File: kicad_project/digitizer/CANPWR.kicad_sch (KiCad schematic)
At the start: 12 parts, among them IC201 MAX3059ASA+T UPSTREAM, IC202 MAX3059ASA+T DOWNSTREAM, IC203 MAX6035AAUR50+T, IC204 MAX6043BAUT33+T, J201 UP_CONN DT15-4P, J202 DOWN_CONN DT06-4S

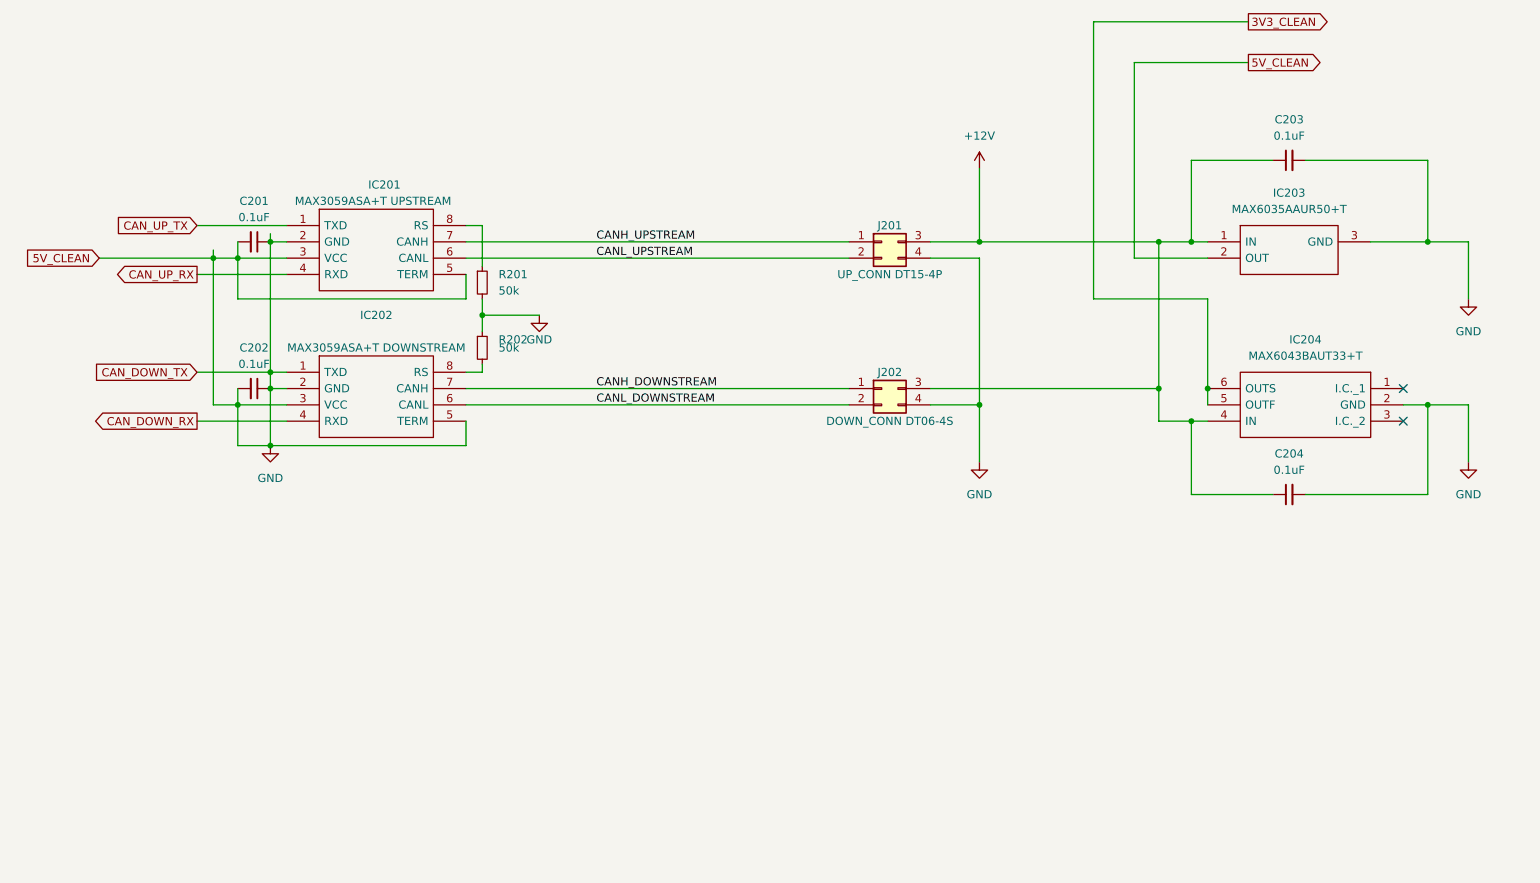
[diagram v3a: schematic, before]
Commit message: added GPIO lines, LED, other small changes
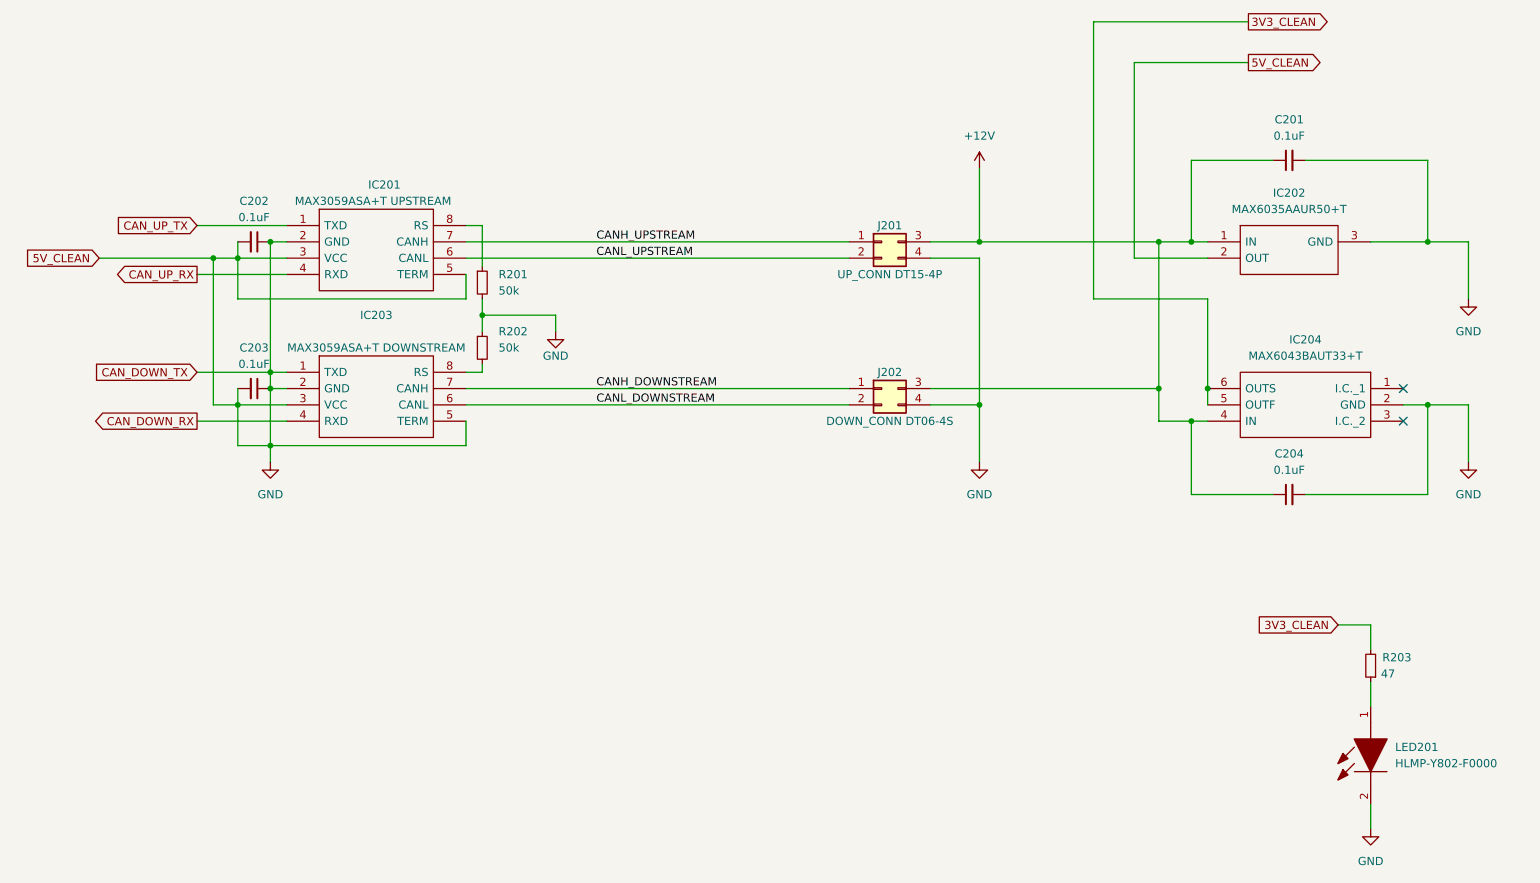
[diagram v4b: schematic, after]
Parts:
- added LED201: HLMP-Y802-F0000, HLMPY802F0000, symbol SamacSys_Parts:HLMP-Y802-F0000
- added R203: 47, Resistor_SMD:R_2512_6332Metric_Pad1.40x3.35mm_HandSolder, symbol Device:R_Small
- renumbered C203 to C201, C201 to C202, C202 to C203, IC203 to IC202, IC202 to IC203
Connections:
- net 3V3_CLEAN: now also R203.2
- net GND: now also LED201.2
- new net: LED201.1, R203.1

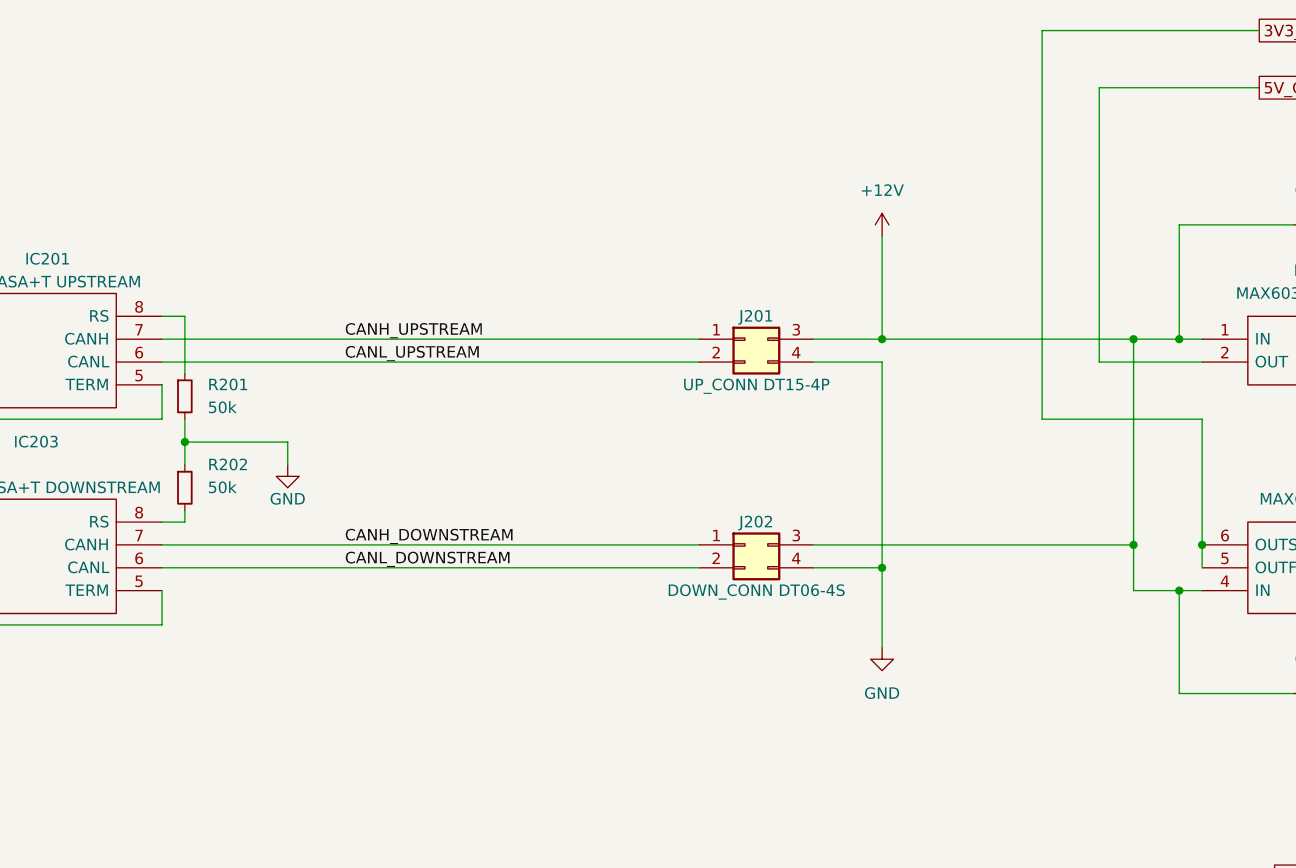
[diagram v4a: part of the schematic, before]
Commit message: added proper connector symbols and footprints for M12 and DT15 (digital upstream) connectors
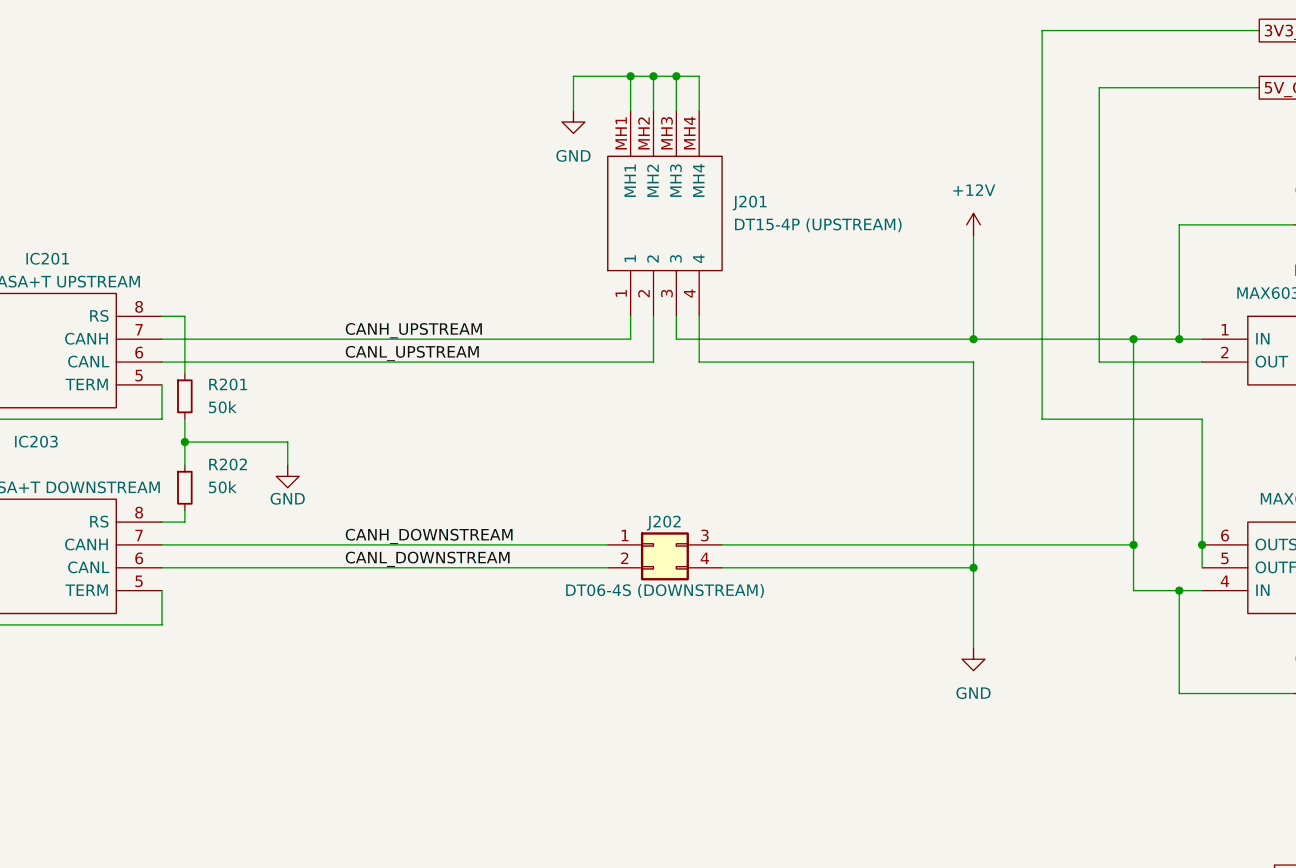
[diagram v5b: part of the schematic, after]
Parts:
- removed J201: UP_CONN DT15-4P, symbol Connector_Generic:Conn_02x02_Top_Bottom
- added J201: DT15-4P (UPSTREAM), DT154P, symbol SamacSys_Parts:DT15-4P
- J202: value DOWN_CONN DT06-4S -> DT06-4S (DOWNSTREAM)
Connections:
- net +12V: now also J201.3
- net CANH_UPSTREAM: now also J201.1
- net CANL_UPSTREAM: now also J201.2
- net GND: now also J201.4, J201.MH1, J201.MH2, J201.MH3, J201.MH4
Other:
- moved on the sheet: J202

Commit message: updated schematic to include terminal blocks for the analog M12 connectors and the downstream CANPWR connector
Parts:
- J202: footprint (none) -> SamacSys_Parts:1935187
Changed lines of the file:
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@@
     (property "Reference" "J202" (id 0) (at 151.13 81.28 0))
     (property "Value" "DT06-4S (DOWNSTREAM)" (id 1) (at 151.13 88.9 0))
-    (property "Footprint" "" (id 2) (at 149.86 83.82 0)
+    (property "Footprint" "SamacSys_Parts:1935187" (id 2) (at 149.86 83.82 0)
       (effects (font (size 1.27 1.27)) hide)
     )

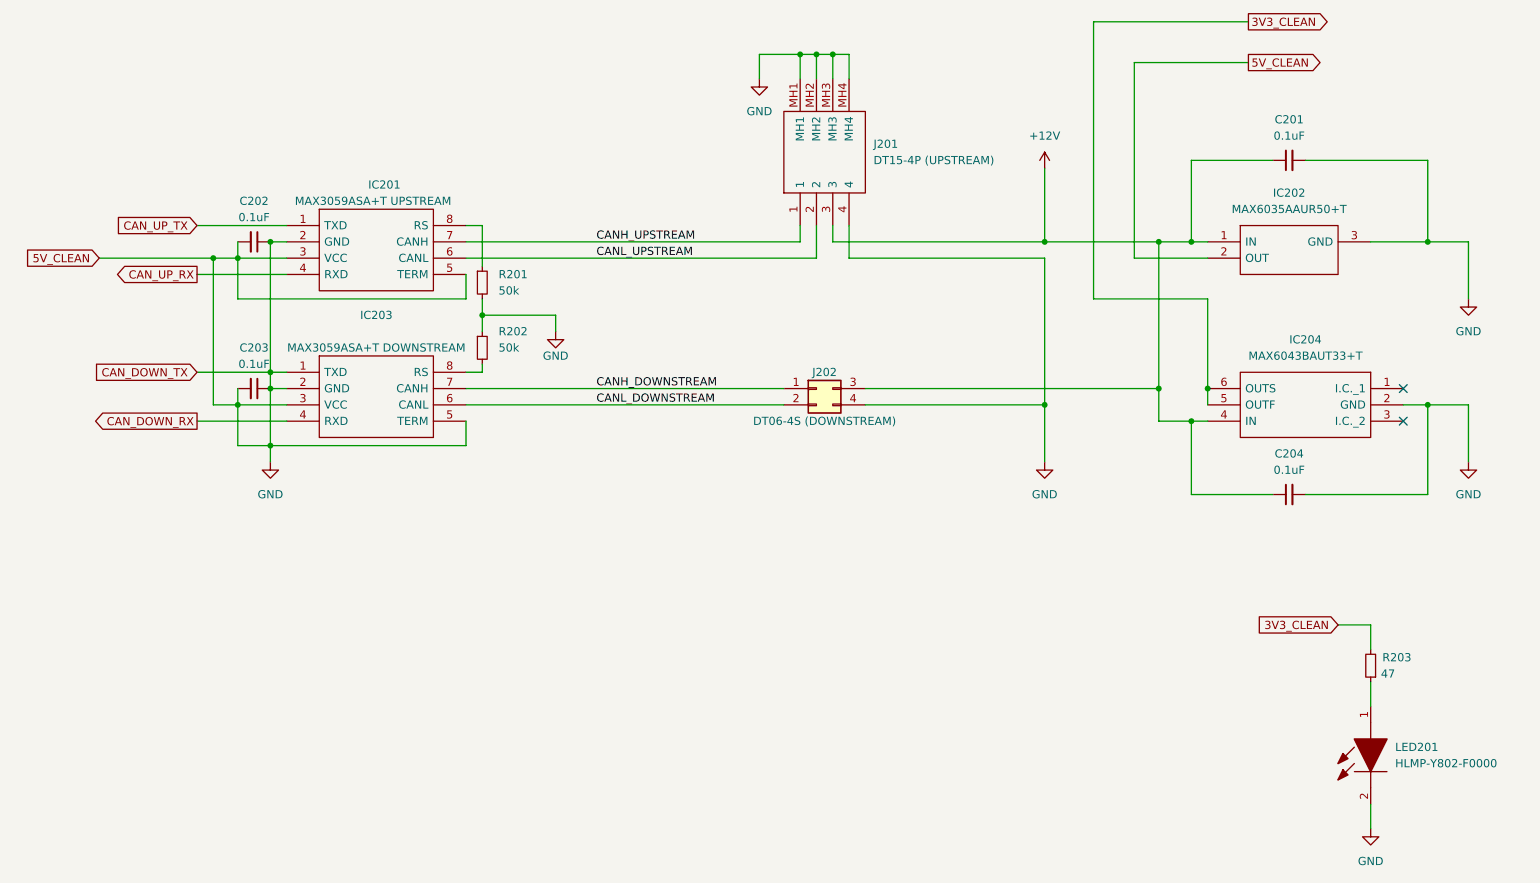
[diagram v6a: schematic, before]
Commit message: cleared ALL errors from electrical rules check; had to explicitly define a bunch of pins, and remove a few bugs (shorted lines, etc.)
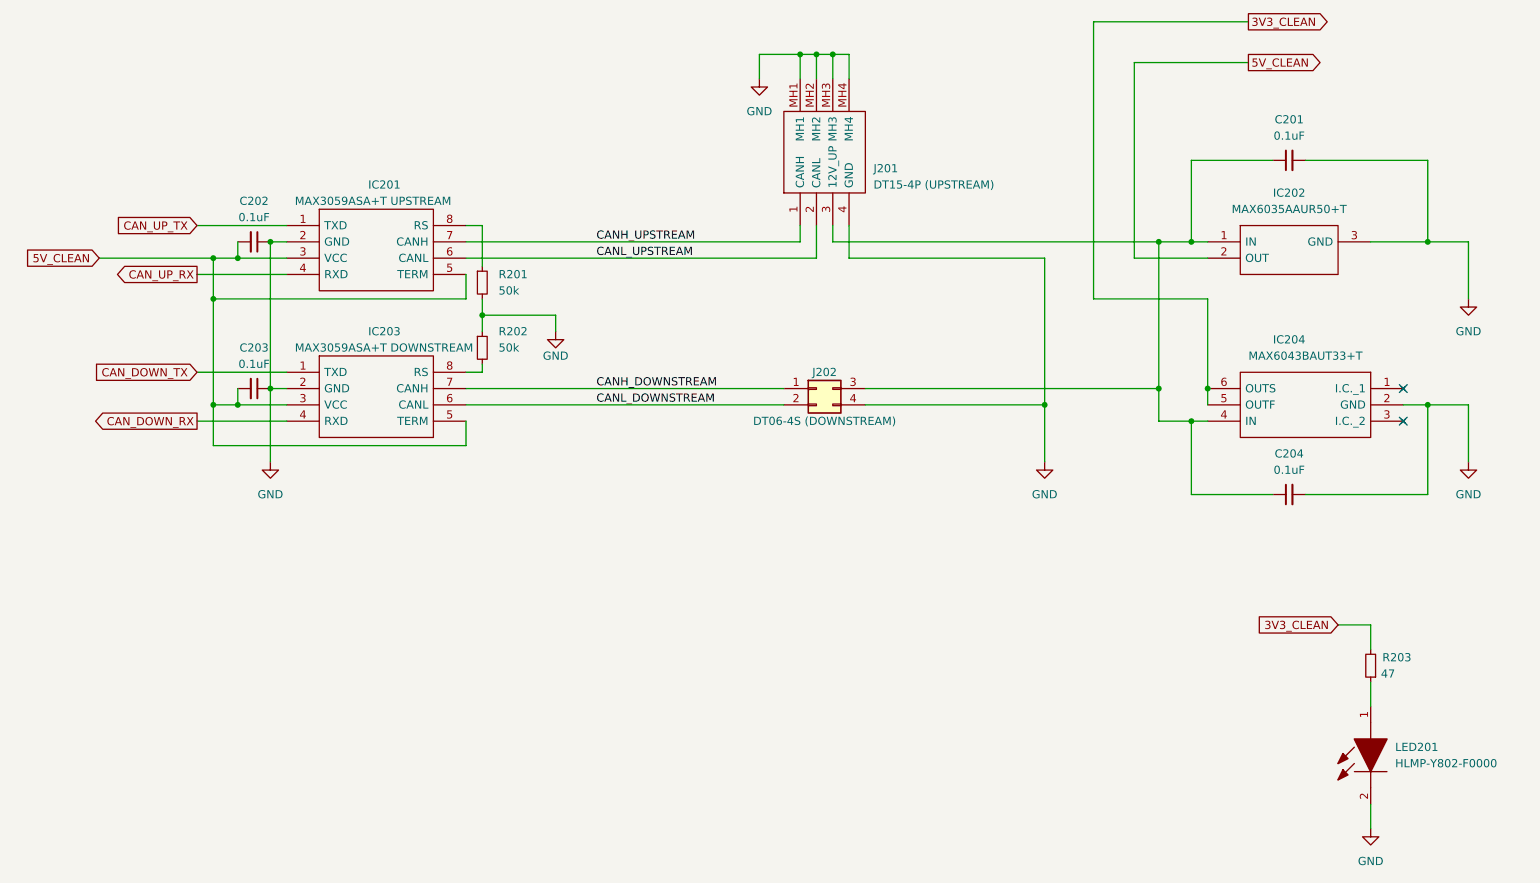
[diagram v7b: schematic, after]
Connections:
- net GND: no longer C202.2, C203.2, IC201.3 (VCC), IC201.5 (TERM), IC202.2 (OUT), IC203.1 (TXD), IC203.3 (VCC), IC203.5 (TERM)
- net +12V: no longer names the net of C201.1, C204.1, IC202.1 (IN), IC204.4 (IN), J201.3 (12V_UP), J202.3 (12V_DOWN)
- new net 5V_CLEAN: C202.2, C203.2, IC201.3 (VCC), IC201.5 (TERM), IC202.2 (OUT), IC203.3 (VCC), IC203.5 (TERM)
- new net CAN_DOWN_TX: IC203.1 (TXD)
